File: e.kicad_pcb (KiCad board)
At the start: 2 copper layers, 115.2 x 78.2 mm, 10 parts, among them SW1 usr, SW2 rst, U1 Display_ST7789, U2 MAX98357A

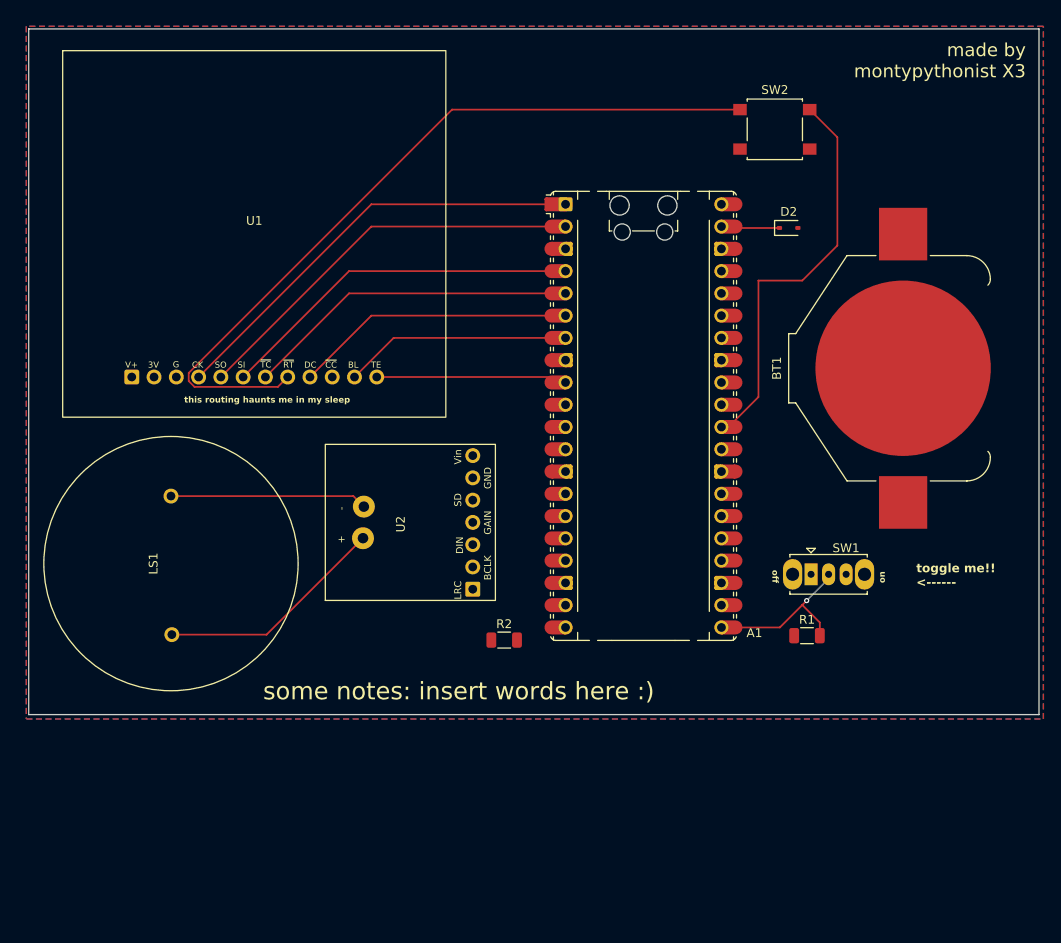
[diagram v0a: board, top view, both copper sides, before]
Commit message: fixed some ERC/DRC errors
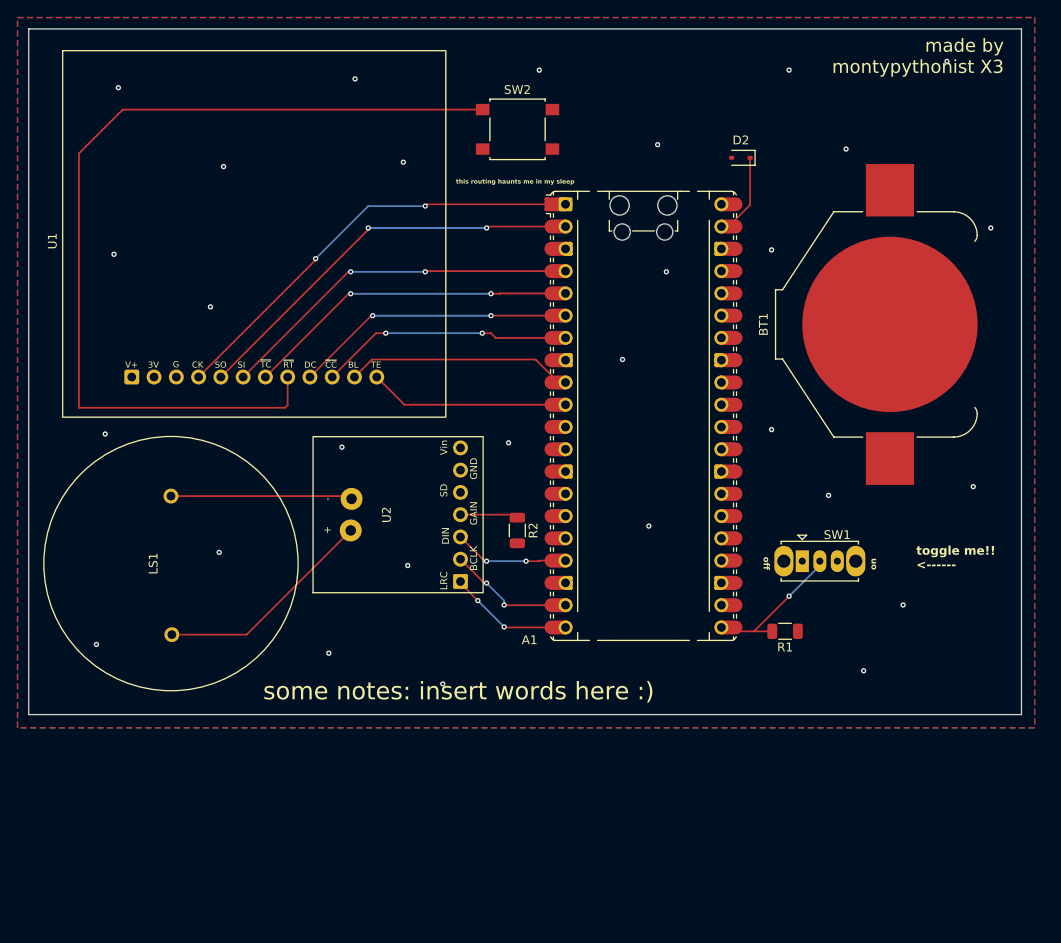
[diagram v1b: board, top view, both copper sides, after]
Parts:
- moved SW2 29.3 mm to (146.0, 53.8)
- moved R2 12.6 mm to (146.0, 99.5), turned to -90 degrees
- moved D2 9.68 mm to (171.5, 57.0), turned to 180 degrees
- moved BT1 5.22 mm to (188.5, 76.0)
- moved R1 2.55 mm to (176.5, 111.0), turned to 180 degrees
- moved U2 1.92 mm to (132.6, 97.7)
- moved SW1 1.80 mm to (178.5, 103.0)
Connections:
- A1 pad 10: unconnected-(A1-GPIO7-Pad10) -> Net-(A1-GPIO7)
- U1 pad 10: (no net) -> Net-(A1-GPIO5)
- U1 pad 11: (no net) -> Net-(A1-GPIO6)
- U1 pad 12: (no net) -> Net-(A1-GPIO7)
- U2 pad 3: (no net) -> Net-(A1-GPIO13)
- U2 pad 4: (no net) -> Net-(U2-GAIN_SLOT)
- U2 pad 5: (no net) -> unconnected-(U2-~{SD_MODE}-Pad5)
- U2 pad 6: (no net) -> GND
- U2 pad 7: (no net) -> +3V0
- U2 pad 8: (no net) -> Net-(U2-OUTP)
- U2 pad 9: (no net) -> Net-(U2-OUTN)
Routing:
- net Net-(A1-RUN): track 133.8 -> 104.2 mm
- net Net-(A1-GPIO7): track 0.00 -> 22.8 mm
- net Net-(A1-GPIO14): track 0.00 -> 13.6 mm, vias 0 -> 2
- net Net-(A1-GPIO15): track 0.00 -> 13.5 mm, vias 0 -> 2
- net Net-(A1-GPIO13): track 0.00 -> 12.3 mm, vias 0 -> 2
- net Net-(U2-GAIN_SLOT): track 0.00 -> 6.62 mm
- net Net-(A1-GPIO6): track 21.0 -> 25.2 mm
- net Net-(A1-VSYS): track 6.69 -> 9.09 mm
- net Net-(A1-GPIO5): track 25.9 -> 28.1 mm, vias 0 -> 2
- net Net-(A1-GPIO16): track 19.1 -> 17.3 mm
- net Net-(U2-OUTP): track 22.5 -> 20.7 mm
- net Net-(U2-OUTN): track 26.4 -> 25.3 mm
- net Net-(A1-GPIO1): track 45.6 -> 45.7 mm, vias 0 -> 2
- net Net-(A1-GPIO0): track 49.2 -> 49.3 mm, vias 0 -> 2
- net Net-(A1-GPIO3): vias 0 -> 2
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- added copper zone on B.Cu, net (none)
- added copper zone on F.Cu, net (none)
- removed copper zone on B.Cu, net GND
- removed copper zone on F.Cu, net GND
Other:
- board size 115.2 x 78.2 mm -> 113.2 x 78.2 mm

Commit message: the board is smaller (but is it cheaper...?)
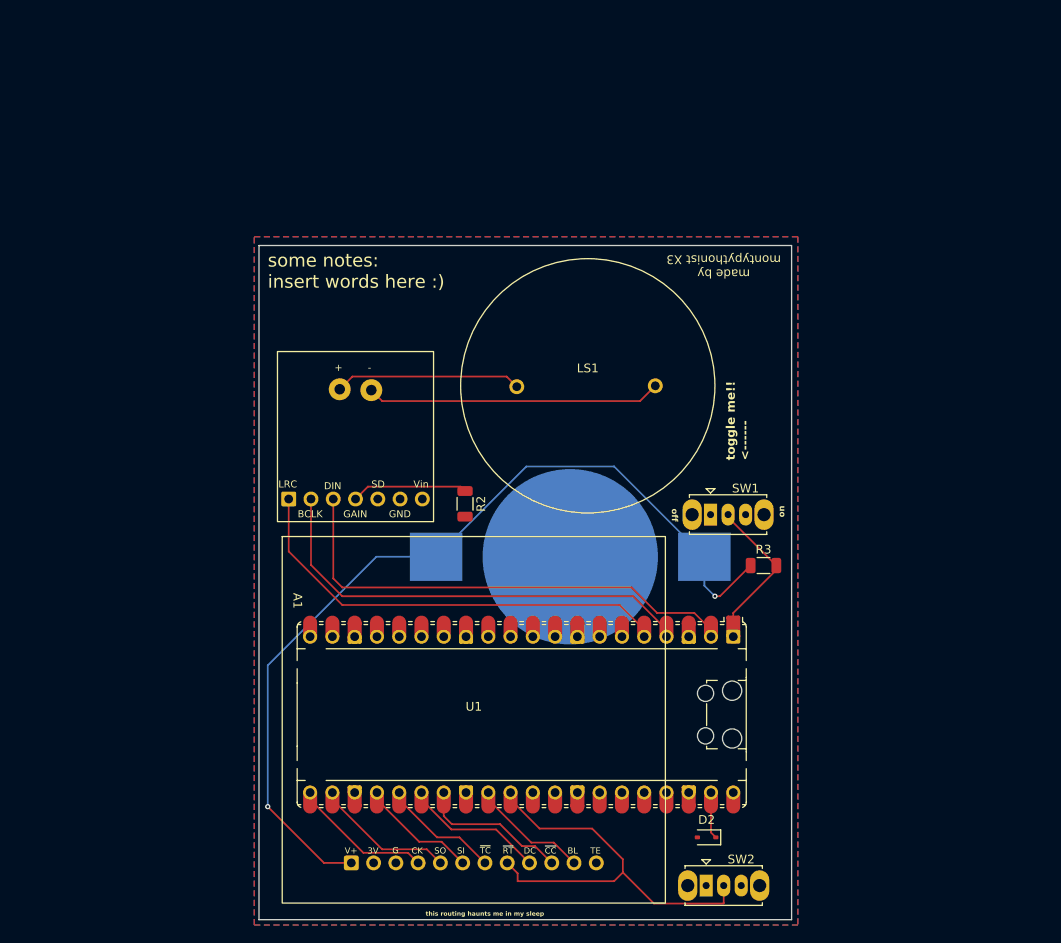
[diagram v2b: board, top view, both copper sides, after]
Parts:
- removed R1: 10K, Resistor_SMD:R_1206_3216Metric
- added R3: 10K, Resistor_SMD:R_1206_3216Metric, F.Cu at (174.1, 103.5)
- BT1: moved to B.Cu
- SW2: footprint Button_Switch_SMD:SW_SPST_B3S-1000 -> Button_Switch_THT:SW_Slide_SPDT_Straight_CK_OS102011MS2Q
- U1: value Display_ST7789 -> ~
- moved SW2 88.9 mm to (167.5, 140.0)
- moved D2 77.6 mm to (167.6, 134.5)
- moved U1 60.8 mm to (141.0, 121.2)
- moved LS1 52.3 mm to (154.0, 82.5), turned to 0 degrees
- moved BT1 45.1 mm to (152.0, 102.5), turned to 0 degrees
- moved A1 36.8 mm to (146.5, 120.5), turned to -90 degrees
- moved SW1 11.7 mm to (168.0, 97.7)
- moved U2 10.1 mm to (127.5, 89.0), turned to 0 degrees
- moved R2 6.69 mm to (140.0, 96.5)
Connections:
- A1 pad 10: Net-(A1-GPIO7) -> unconnected-(A1-GPIO7-Pad10)
- A1 pad 17: Net-(A1-GPIO13) -> unconnected-(A1-GPIO13-Pad17)_1
- A1 pad 19: Net-(A1-GPIO14) -> unconnected-(A1-GPIO14-Pad19)
- A1 pad 20: Net-(A1-GPIO15) -> unconnected-(A1-GPIO15-Pad20)_1
- A1 pad 22: unconnected-(A1-GPIO17-Pad22)_1 -> Net-(A1-GPIO17)
- A1 pad 24: unconnected-(A1-GPIO18-Pad24)_1 -> Net-(A1-GPIO18)
- A1 pad 25: unconnected-(A1-GPIO19-Pad25) -> Net-(A1-GPIO19)
- A1 pad 26: unconnected-(A1-GPIO20-Pad26) -> Net-(A1-GPIO20)
- A1 pad 27: unconnected-(A1-GPIO21-Pad27)_1 -> Net-(A1-GPIO21)
- A1 pad 29: unconnected-(A1-GPIO22-Pad29) -> Net-(A1-GPIO22)
- A1 pad 6: Net-(A1-GPIO4) -> unconnected-(A1-GPIO4-Pad6)_1
- A1 pad 7: Net-(A1-GPIO5) -> unconnected-(A1-GPIO5-Pad7)
- A1 pad 9: Net-(A1-GPIO6) -> unconnected-(A1-GPIO6-Pad9)
- SW1 pad 2: Net-(A1-GPIO16) -> Net-(A1-GPIO0)
- SW2 pad 1: Net-(A1-RUN) -> GND
- SW2 pad 2: GND -> Net-(A1-RUN)
- U1 pad 10: Net-(A1-GPIO5) -> Net-(A1-GPIO21)
- U1 pad 11: Net-(A1-GPIO6) -> Net-(A1-GPIO22)
- U1 pad 12: Net-(A1-GPIO7) -> (no net)
- U1 pad 4: Net-(A1-GPIO0) -> Net-(A1-GPIO16)
- U1 pad 5: Net-(A1-GPIO1) -> Net-(A1-GPIO17)
- U1 pad 6: Net-(A1-GPIO2) -> Net-(A1-GPIO18)
- U1 pad 7: Net-(A1-GPIO3) -> Net-(A1-GPIO19)
- U1 pad 9: Net-(A1-GPIO4) -> Net-(A1-GPIO20)
- U2 pad 1: Net-(A1-GPIO15) -> Net-(A1-GPIO3)
- U2 pad 2: Net-(A1-GPIO14) -> Net-(A1-GPIO2)
- U2 pad 3: Net-(A1-GPIO13) -> Net-(A1-GPIO1)
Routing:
- net +3V0: track 0.00 -> 102.3 mm, vias 0 -> 2
- net Net-(A1-RUN): track 104.2 -> 47.1 mm
- net Net-(A1-GPIO4): track 31.2 -> 0.00 mm, vias 2 -> 0
- net Net-(A1-GPIO0): track 49.3 -> 18.2 mm, vias 2 -> 0
- net Net-(A1-GPIO5): track 28.1 -> 0.00 mm, vias 2 -> 0
- net Net-(A1-GPIO6): track 25.2 -> 0.00 mm
- net Net-(A1-GPIO7): track 22.8 -> 0.00 mm
- net Net-(A1-GPIO21): track 0.00 -> 16.4 mm
- net Net-(A1-GPIO20): track 0.00 -> 15.3 mm
- net Net-(A1-GPIO17): track 0.00 -> 15.3 mm
- net Net-(A1-GPIO14): track 13.6 -> 0.00 mm, vias 2 -> 0
- net Net-(A1-GPIO15): track 13.5 -> 0.00 mm, vias 2 -> 0
- net Net-(U2-OUTP): track 20.7 -> 33.6 mm
- net Net-(A1-GPIO3): track 37.4 -> 50.2 mm, vias 2 -> 0
- net Net-(A1-GPIO22): track 0.00 -> 12.8 mm
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- added copper zone on B.Cu, net GND
- added copper zone on F.Cu, net GND
- removed copper zone on B.Cu, net (none)
- removed copper zone on F.Cu, net (none)
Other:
- board size 113.2 x 78.2 mm -> 60.7 x 76.9 mm

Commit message: the board is smaller... and cooler... and slightly cheaper!!
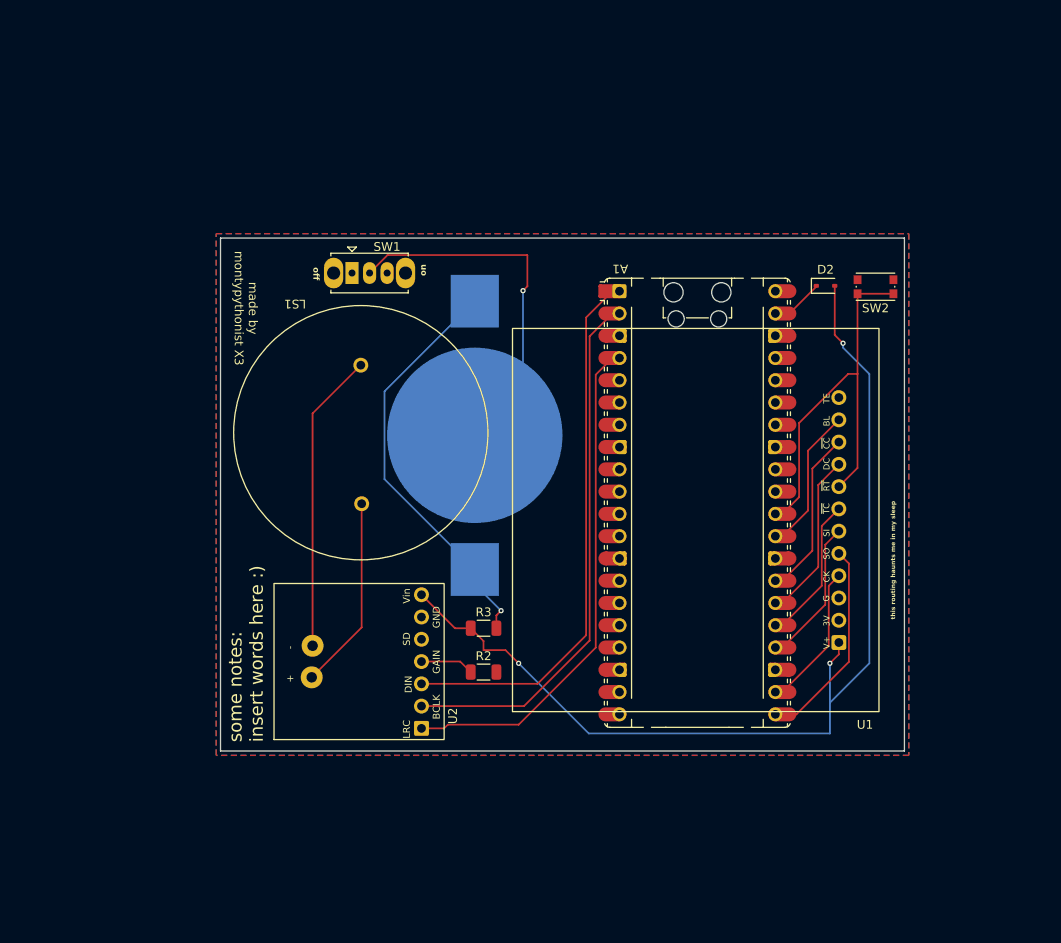
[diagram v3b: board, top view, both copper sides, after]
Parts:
- SW2: footprint Button_Switch_THT:SW_Slide_SPDT_Straight_CK_OS102011MS2Q -> Button_Switch_SMD:SW_Push_1P1T_NO_CK_KMR2
- U1: value ~ -> Display_ST7789
- moved SW2 71.0 mm to (186.8, 71.7), turned to 180 degrees
- moved D2 64.3 mm to (181.2, 71.6), turned to 0 degrees
- moved SW1 49.3 mm to (127.2, 70.1)
- moved U1 34.2 mm to (166.4, 98.3), turned to 90 degrees
- moved R3 32.7 mm to (142.2, 110.7)
- moved A1 31.4 mm to (166.5, 96.3), turned to 0 degrees
- moved LS1 27.0 mm to (127.7, 88.3), turned to 90 degrees
- moved U2 25.5 mm to (128.2, 114.5), turned to 90 degrees
- moved R2 19.3 mm to (142.2, 115.7), turned to 0 degrees
- moved BT1 17.6 mm to (141.2, 88.7), turned to -90 degrees
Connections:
- A1 pad 5: Net-(A1-GPIO3) -> unconnected-(A1-GPIO3-Pad5)
- BT1 pad 1: +3V0 -> Net-(BT1-+)
- BT1 pad 2: GND -> Net-(BT1--)
- R3 pad 2: Net-(A1-GPIO0) -> Net-(BT1-+)
- SW1 pad 2: Net-(A1-GPIO0) -> Net-(BT1--)
- SW2 pad 1: GND -> Net-(A1-RUN)
- SW2 pad 2: Net-(A1-RUN) -> GND
- U1 pad 4: Net-(A1-GPIO16) -> Net-(A1-GPIO17)
- U1 pad 5: Net-(A1-GPIO17) -> Net-(A1-GPIO16)
- U2 pad 1: Net-(A1-GPIO3) -> Net-(A1-GPIO2)
- U2 pad 2: Net-(A1-GPIO2) -> Net-(A1-GPIO1)
- U2 pad 3: Net-(A1-GPIO1) -> Net-(A1-GPIO0)
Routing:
- net Net-(A1-GPIO3): track 50.2 -> 0.00 mm
- net Net-(BT1-+): track 0.00 -> 47.3 mm, vias 0 -> 1
- net Net-(BT1--): track 0.00 -> 45.4 mm, vias 0 -> 1
- net Net-(A1-GPIO0): track 18.2 -> 61.6 mm
- net +3V0: track 102.3 -> 115.6 mm, vias 2 -> 3
- net Net-(A1-GPIO16): track 15.3 -> 22.9 mm
- net Net-(U2-GAIN_SLOT): track 13.3 -> 6.11 mm
- net Net-(A1-GPIO2): track 51.1 -> 57.5 mm
- net Net-(A1-GPIO1): track 54.6 -> 60.7 mm
- net Net-(A1-GPIO20): track 15.3 -> 18.5 mm
- net Net-(A1-GPIO22): track 12.8 -> 15.9 mm
- net Net-(A1-GPIO18): track 12.8 -> 15.9 mm
- net Net-(A1-GPIO19): track 12.8 -> 15.9 mm
- net Net-(A1-GPIO21): track 16.4 -> 18.5 mm
- net Net-(U2-OUTN): track 21.3 -> 22.2 mm
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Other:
- board size 60.7 x 76.9 mm -> 78 x 58.5 mm
- board text removed: "toggle me!! <------"
